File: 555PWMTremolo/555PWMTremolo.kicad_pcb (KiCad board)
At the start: 2 copper layers, 54.6 x 98.6 mm, 40 parts

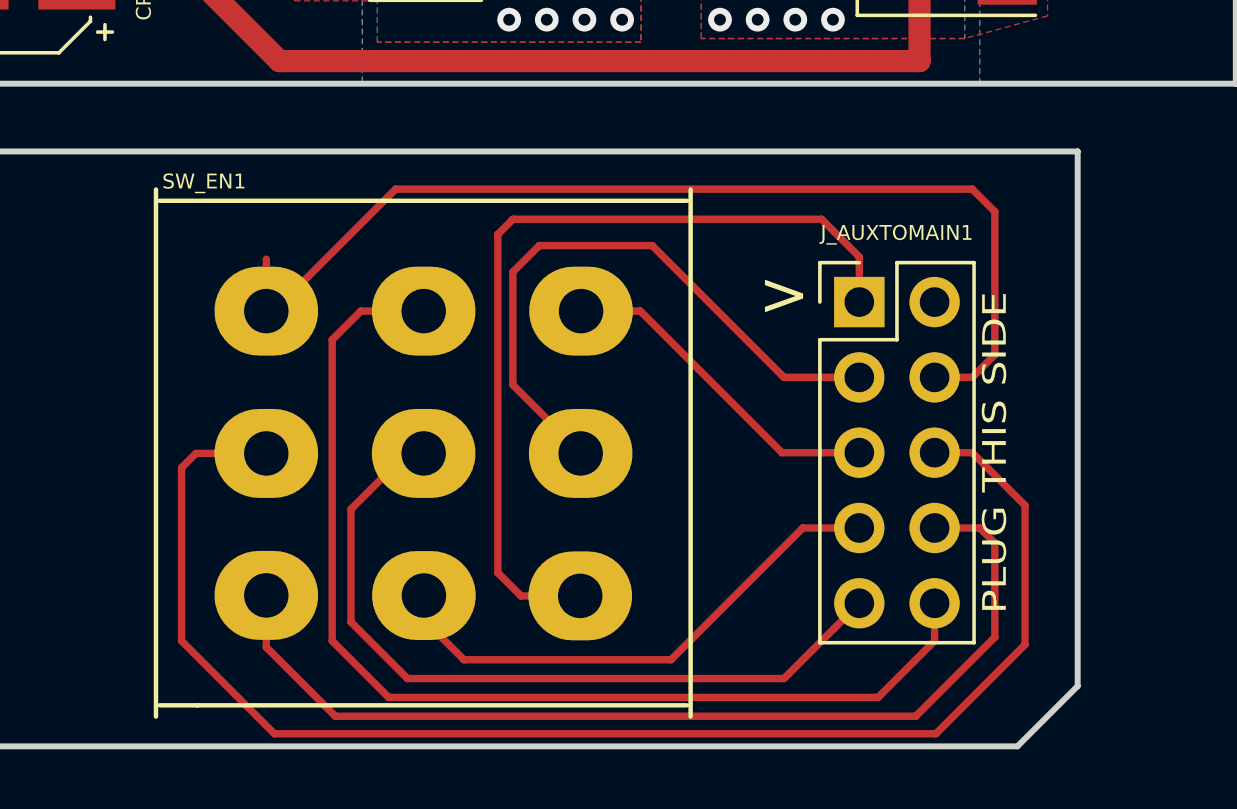
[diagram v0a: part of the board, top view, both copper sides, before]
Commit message: Board Layout Corrections
Aux Board Ribbon cable header inversed
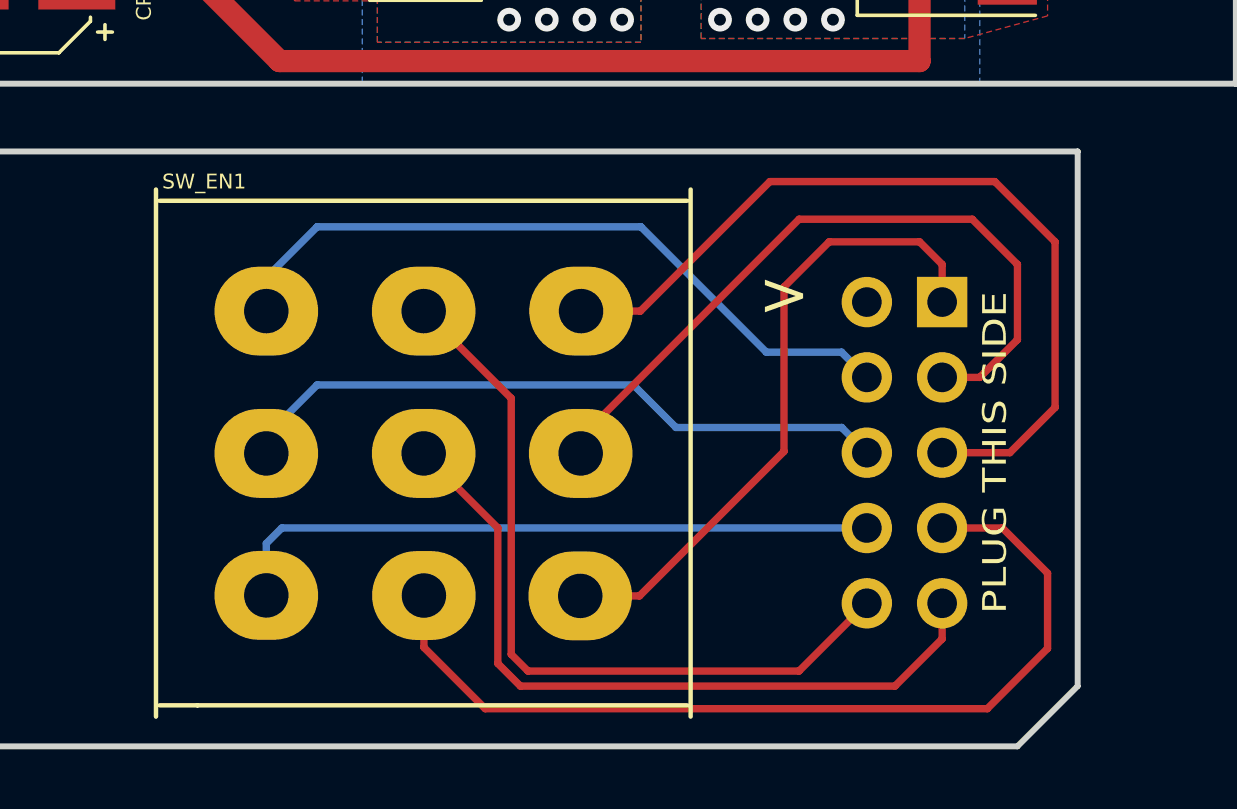
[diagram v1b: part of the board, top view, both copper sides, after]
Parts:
- J_AUXTOMAIN1: moved to B.Cu
- moved J_AUXTOMAIN1 2.79 mm to (98.0, 154.9), turned to 180 degrees
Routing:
- net /555PWMTremolo_3PDT/3PDT_8_INT: track 48.7 -> 22.8 mm
- net /555PWMTremolo_3PDT/3PDT_3_INT: track 11.4 -> 28.7 mm
- net /555PWMTremolo_3PDT/3PDT_4_INT: track 17.9 -> 31.2 mm
- net /555PWMTremolo_3PDT/3PDT_7_INT: track 33.8 -> 22.2 mm
- net /555PWMTremolo_3PDT/3PDT_9_INT: track 35.5 -> 24.2 mm
- net /555PWMTremolo_3PDT/3PDT_6_INT: track 36.8 -> 26.0 mm
- net /555PWMTremolo_3PDT/3PDT_1_INT: track 29.0 -> 22.0 mm
- net /555PWMTremolo_3PDT/3PDT_2_INT: track 21.0 -> 24.6 mm
- net /555PWMTremolo_3PDT/3PDT_5_INT: track 26.0 -> 25.3 mm

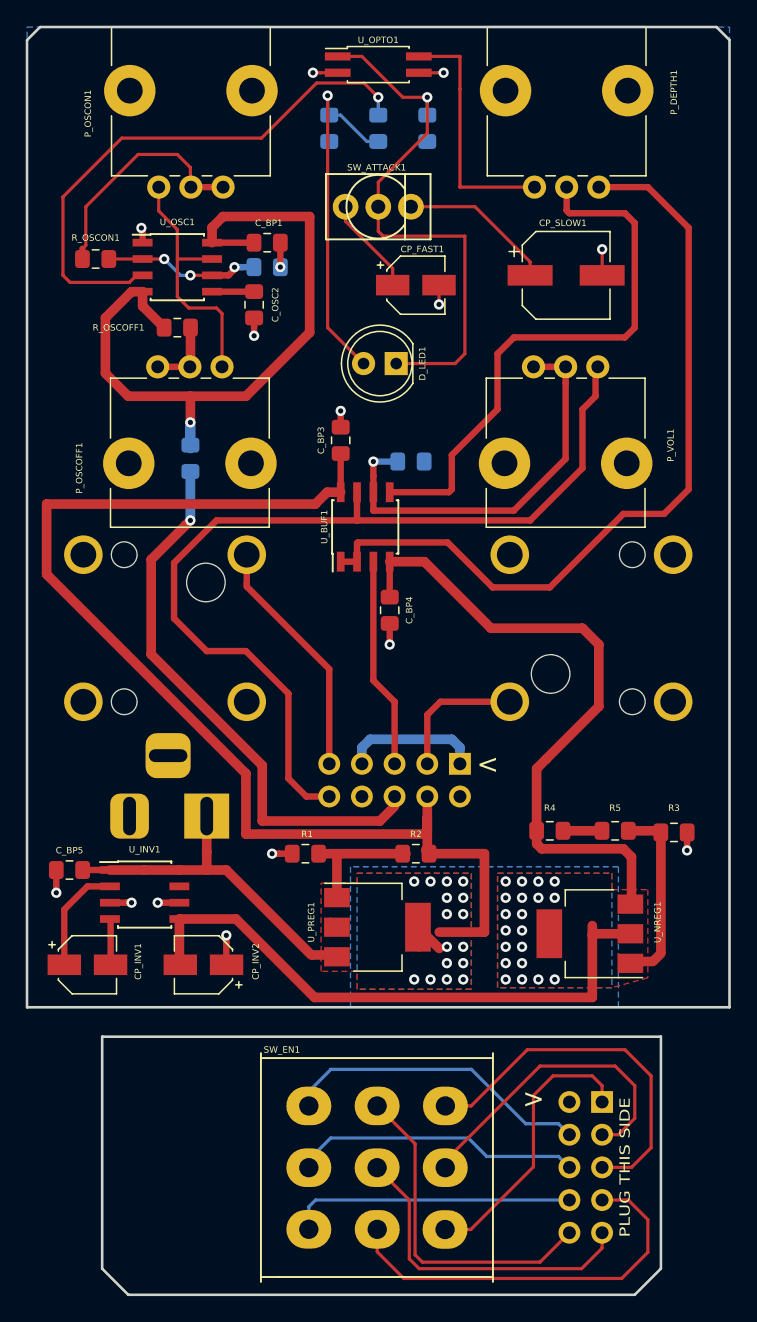
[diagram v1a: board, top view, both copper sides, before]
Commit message: Added second 555 IC bypass cap
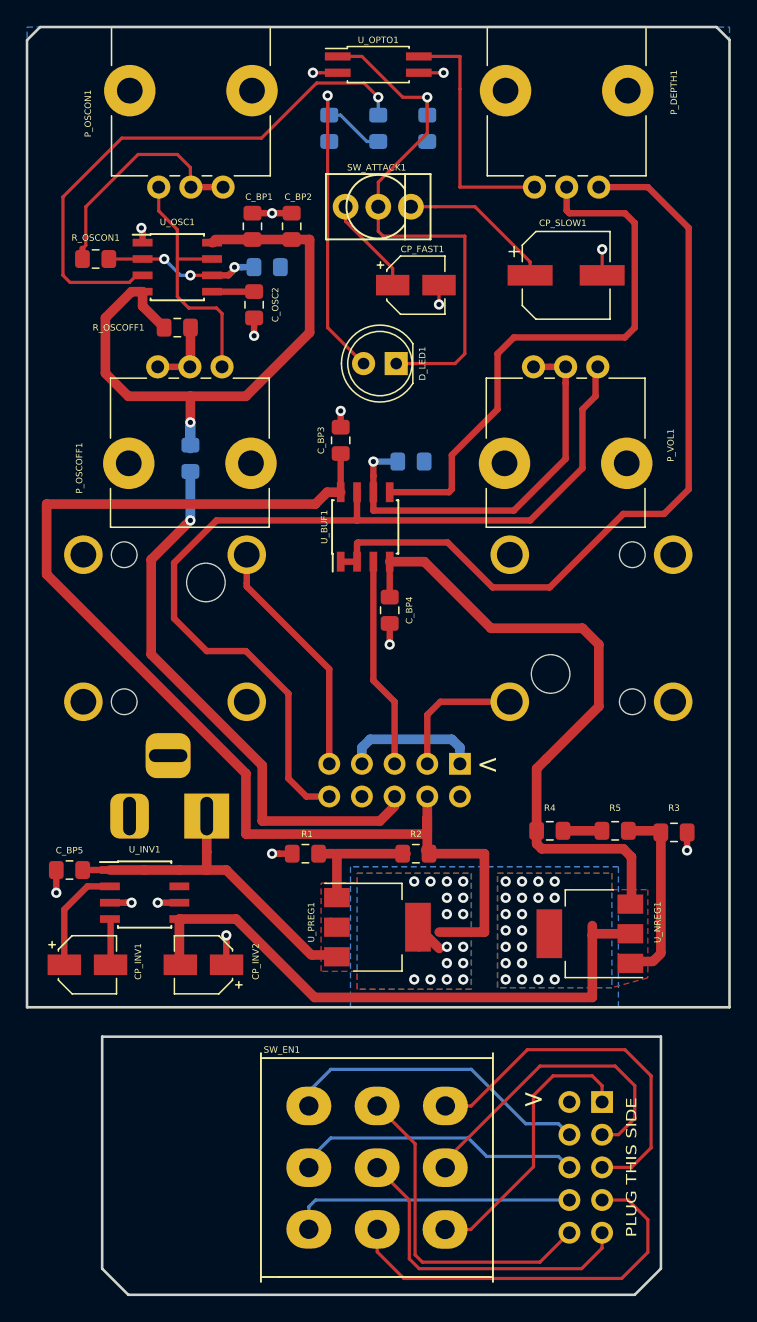
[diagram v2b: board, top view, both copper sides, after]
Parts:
- added C_BP2: 47uF, Capacitor_SMD:C_0805_2012Metric_Pad1.15x1.40mm_HandSolder, F.Cu at (73.9, 86.9)
- R_GAIN1: value 3K9 -> 2K7
- R_OSCLIMIT1: value 100R -> 330R
- R_OSCOFF1, R_OSCON1: value 100R -> 220R
- moved C_BP1 1.71 mm to (70.9, 86.9), turned to 90 degrees
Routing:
- net Net-(C_BP1-Pad1): track 57.4 -> 51.1 mm
- net /GND: track 25.5 -> 26.6 mm
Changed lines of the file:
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@@
-(kicad_pcb (version 20171130) (host pcbnew "(5.0.0)")
+(kicad_pcb (version 20171130) (host pcbnew "(5.0.0-3-g5ebb6b6)")
   (general
     (thickness 1.6)
     (drawings 27)
-    (tracks 392)
+    (tracks 393)
     (zones 0)
-    (modules 40)
+    (modules 41)
     (nets 41)
   )
@@
   )
   (setup
-    (last_trace_width 0.25)
+    (last_trace_width 0.5)
     (user_trace_width 0.5)
     (user_trace_width 0.75)
@@
       (effects (font (size 0.5 0.5) (thickness 0.125)) (justify mirror))
     )
-    (fp_text value 3K9 (at 0 -1.65) (layer B.Fab)
+    (fp_text value 2K7 (at 0 -1.65) (layer B.Fab)
       (effects (font (size 0.5 0.5) (thickness 0.125)) (justify mirror))
     )
@@
   )
   (module Capacitor_SMD:C_0805_2012Metric_Pad1.15x1.40mm_HandSolder (layer F.Cu)
-    (at 72.009 88.138)
+    (at 70.866 86.868 90)
     (descr "Capacitor SMD 0805 (2012 Metric), square (rectangular) end terminal, IPC_7351 nominal with elongated pad for handsoldering. (Body size source: https://docs.google.com/spreadsheets/d/1BsfQQcO9C6DZCsRaXUlFlo91Tg2WpOkGARC1WS5S8t0/edit?usp=sharing), generated with kicad-footprint-generator")
     (tags "capacitor handsolder")
     (attr smd)
-    (fp_text reference C_BP1 (at 0.127 -1.524 180) (layer F.SilkS)
-      (effects (font (size 0.5 0.5) (thickness 0.125)))
-    )
-    (fp_text value 100nF (at 0 1.65) (layer F.Fab)
+    (fp_text reference C_BP1 (at 2.286 0.508 180) (layer F.SilkS)
+      (effects (font (size 0.5 0.5) (thickness 0.125)))
+    )
+    (fp_text value 100nF (at 0 1.65 90) (layer F.Fab)
       (effects (font (size 0.5 0.5) (thickness 0.125)))
     )
@@
     (fp_line (start 1.85 -0.95) (end 1.85 0.95) (layer F.CrtYd) (width 0.05))
     (fp_line (start 1.85 0.95) (end -1.85 0.95) (layer F.CrtYd) (width 0.05))
-    (fp_text user %R (at 0 0) (layer F.Fab)
-      (effects (font (size 0.5 0.5) (thickness 0.125)))
-    )
-    (pad 1 smd roundrect (at -1.025 0) (size 1.15 1.4) (layers F.Cu F.Paste F.Mask) (roundrect_rratio 0.217391)
+    (fp_text user %R (at 0 0 90) (layer F.Fab)
+      (effects (font (size 0.5 0.5) (thickness 0.125)))
+    )
+    (pad 1 smd roundrect (at -1.025 0 90) (size 1.15 1.4) (layers F.Cu F.Paste F.Mask) (roundrect_rratio 0.217391)
       (net 37 "Net-(C_BP1-Pad1)"))
-    (pad 2 smd roundrect (at 1.025 0) (size 1.15 1.4) (layers F.Cu F.Paste F.Mask) (roundrect_rratio 0.217391)
+    (pad 2 smd roundrect (at 1.025 0 90) (size 1.15 1.4) (layers F.Cu F.Paste F.Mask) (roundrect_rratio 0.217391)
       (net 36 /GND))
     (model ${KISYS3DMOD}/Capacitor_SMD.3dshapes/C_0805_2012Metric.wrl
@@
       (effects (font (size 0.5 0.5) (thickness 0.125)))
     )
-    (fp_text value 100R (at 0 1.65 180) (layer F.Fab)
+    (fp_text value 220R (at 0 1.65 180) (layer F.Fab)
       (effects (font (size 0.5 0.5) (thickness 0.125)))
     )
@@
       (effects (font (size 0.5 0.5) (thickness 0.125)))
     )
-    (fp_text value 100R (at 0 1.65) (layer F.Fab)
+    (fp_text value 220R (at 0 1.65) (layer F.Fab)
       (effects (font (size 0.5 0.5) (thickness 0.125)))
     )
@@
       (effects (font (size 0.5 0.5) (thickness 0.125)) (justify mirror))
     )
-    (fp_text value 100R (at 0 -1.65 90) (layer B.Fab)
+    (fp_text value 330R (at 0 -1.65 90) (layer B.Fab)
       (effects (font (size 0.5 0.5) (thickness 0.125)) (justify mirror))
     )
@@
     )
   )
+  (module Capacitor_SMD:C_0805_2012Metric_Pad1.15x1.40mm_HandSolder (layer F.Cu)
+    (at 73.914 86.868 90)
+    (descr "Capacitor SMD 0805 (2012 Metric), square (rectangular) end terminal, IPC_7351 nominal with elongated pad for handsoldering. (Body size source: https://docs.google.com/spreadsheets/d/1BsfQQcO9C6DZCsRaXUlFlo91Tg2WpOkGARC1WS5S8t0/edit?usp=sharing), generated with kicad-footprint-generator")
+    (tags "capacitor handsolder")
+    (attr smd)
+    (fp_text reference C_BP2 (at 2.286 0.508 180) (layer F.SilkS)
+      (effects (font (size 0.5 0.5) (thickness 0.125)))
+    )
+    (fp_text value 47uF (at 0 1.65 90) (layer F.Fab)
+      (effects (font (size 0.5 0.5) (thickness 0.125)))
+    )
+    (fp_line (start -1 0.6) (end -1 -0.6) (layer F.Fab) (width 0.1))
+    (fp_line (start -1 -0.6) (end 1 -0.6) (layer F.Fab) (width 0.1))
+    (fp_line (start 1 -0.6) (end 1 0.6) (layer F.Fab) (width 0.1))
+    (fp_line (start 1 0.6) (end -1 0.6) (layer F.Fab) (width 0.1))
+    (fp_line (start -0.261252 -0.71) (end 0.261252 -0.71) (layer F.SilkS) (width 0.12))
+    (fp_line (start -0.261252 0.71) (end 0.261252 0.71) (layer F.SilkS) (width 0.12))
+    (fp_line (start -1.85 0.95) (end -1.85 -0.95) (layer F.CrtYd) (width 0.05))
+    (fp_line (start -1.85 -0.95) (end 1.85 -0.95) (layer F.CrtYd) (width 0.05))
+    (fp_line (start 1.85 -0.95) (end 1.85 0.95) (layer F.CrtYd) (width 0.05))
+    (fp_line (start 1.85 0.95) (end -1.85 0.95) (layer F.CrtYd) (width 0.05))
+    (fp_text user %R (at 0 0 90) (layer F.Fab)
+      (effects (font (size 0.5 0.5) (thickness 0.125)))
+    )
+    (pad 1 smd roundrect (at -1.025 0 90) (size 1.15 1.4) (layers F.Cu F.Paste F.Mask) (roundrect_rratio 0.217391)
+      (net 37 "Net-(C_BP1-Pad1)"))
+    (pad 2 smd roundrect (at 1.025 0 90) (size 1.15 1.4) (layers F.Cu F.Paste F.Mask) (roundrect_rratio 0.217391)
+      (net 36 /GND))
+    (model ${KISYS3DMOD}/Capacitor_SMD.3dshapes/C_0805_2012Metric.wrl
+      (at (xyz 0 0 0))
+      (scale (xyz 1 1 1))
+      (rotate (xyz 0 0 0))
+    )
+  )
   (gr_text "higher val \nlower range" (at 71.882 87.122) (layer B.SilkS)
     (effects (font (size 0.8 0.8) (thickness 0.1)) (justify mirror))
@@
     (effects (font (size 1.5 1.5) (thickness 0.3)))
   )
-  (gr_text "PLUG THIS SIDE" (at 99.822 160.02 90) (layer F.SilkS)
+  (gr_text "PLUG THIS SIDE" (at 100.33 160.02 90) (layer F.SilkS)
     (effects (font (size 0.8 1) (thickness 0.2)))
   )
@@
   (via (at 70.993 95.377) (size 0.8) (drill 0.4) (layers F.Cu B.Cu) (net 36))
   (segment (start 70.993 94.664) (end 70.993 95.377) (width 0.5) (layer F.Cu) (net 36))
-  (segment (start 73.034 88.138) (end 73.034 90.034) (width 0.5) (layer F.Cu) (net 36))
-  (via (at 73.034 90.034) (size 0.8) (drill 0.4) (layers F.Cu B.Cu) (net 36))
+  (via (at 72.39 85.852) (size 0.8) (drill 0.4) (layers F.Cu B.Cu) (net 36))
   (segment (start 77.724 102.48) (end 77.724 101.219) (width 0.5) (layer F.Cu) (net 36))
   (via (at 77.724 101.219) (size 0.8) (drill 0.4) (layers F.Cu B.Cu) (net 36))
@@
   (via (at 81.534 119.38) (size 0.8) (drill 0.4) (layers F.Cu B.Cu) (net 36))
   (segment (start 81.534 117.738) (end 81.534 119.38) (width 0.5) (layer F.Cu) (net 36))
+  (segment (start 70.866 85.843) (end 73.914 85.843) (width 0.5) (layer F.Cu) (net 36))
   (segment (start 59.436 93.98) (end 59.436 98.298) (width 0.75) (layer F.Cu) (net 37))
   (segment (start 59.436 98.298) (end 61.214 100.076) (width 0.75) (layer F.Cu) (net 37))
@@
   (segment (start 62.324 93.067) (end 63.999 94.742) (width 0.75) (layer F.Cu) (net 37))
   (segment (start 62.324 91.948) (end 62.324 93.067) (width 0.75) (layer F.Cu) (net 37))
-  (segment (start 67.724 86.962) (end 67.724 88.138) (width 0.75) (layer F.Cu) (net 37))
-  (segment (start 68.58 86.106) (end 67.724 86.962) (width 0.75) (layer F.Cu) (net 37))
-  (segment (start 75.311 86.106) (end 68.58 86.106) (width 0.75) (layer F.Cu) (net 37))
-  (segment (start 75.311 95.123) (end 75.311 86.106) (width 0.75) (layer F.Cu) (net 37))
+  (segment (start 67.818 88.138) (end 67.724 88.138) (width 0.75) (layer F.Cu) (net 37))
   (segment (start 70.358 100.076) (end 75.311 95.123) (width 0.75) (layer F.Cu) (net 37))
   (segment (start 66.04 100.076) (end 70.358 100.076) (width 0.75) (layer F.Cu) (net 37))
-  (segment (start 67.724 88.138) (end 70.993 88.138) (width 0.5) (layer F.Cu) (net 37))
+  (segment (start 67.969 87.893) (end 67.724 88.138) (width 0.5) (layer F.Cu) (net 37))
+  (segment (start 73.914 87.893) (end 67.969 87.893) (width 0.75) (layer F.Cu) (net 37))
+  (segment (start 75.302 87.893) (end 75.311 87.884) (width 0.5) (layer F.Cu) (net 37))
+  (segment (start 73.914 87.893) (end 75.302 87.893) (width 0.75) (layer F.Cu) (net 37))
+  (segment (start 75.311 95.123) (end 75.311 87.884) (width 0.75) (layer F.Cu) (net 37))
   (via (at 84.455 76.835) (size 0.8) (drill 0.4) (layers F.Cu B.Cu) (net 38))
   (segment (start 84.455 76.835) (end 82.55 76.835) (width 0.25) (layer F.Cu) (net 38))
